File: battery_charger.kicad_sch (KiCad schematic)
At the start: 29 parts, among them J8 Conn_01x04, U15 BQ25895RTW, U17 NX3DV42GU, U18 MP3422GG-P, U20 MAX16150A

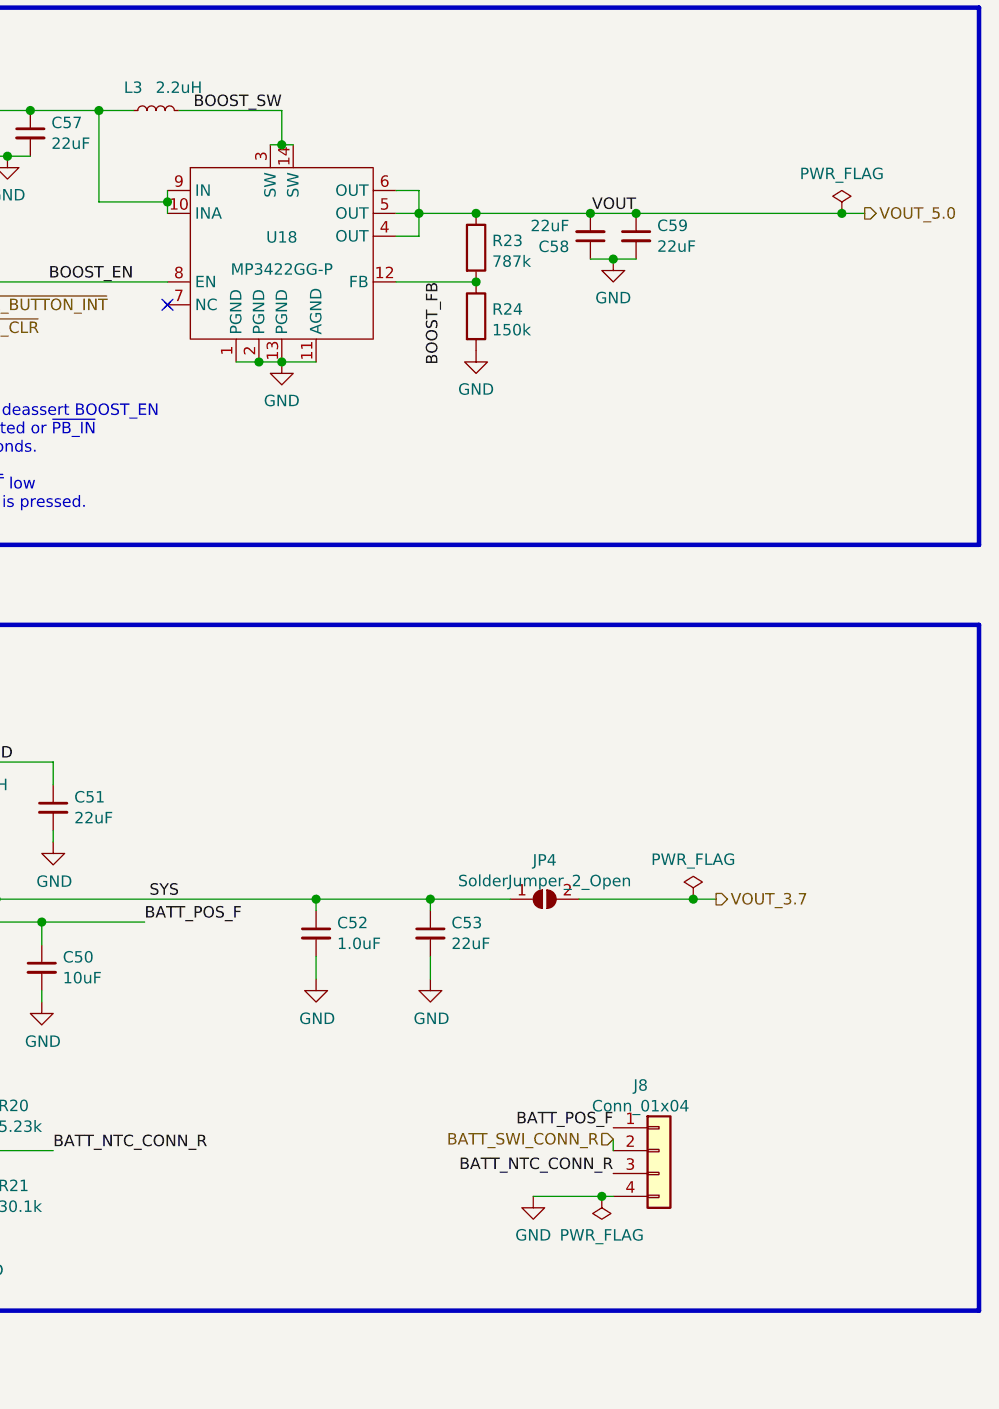
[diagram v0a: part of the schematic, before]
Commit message: Fix most ERC errors; cleanup silkscreen and comment layers.
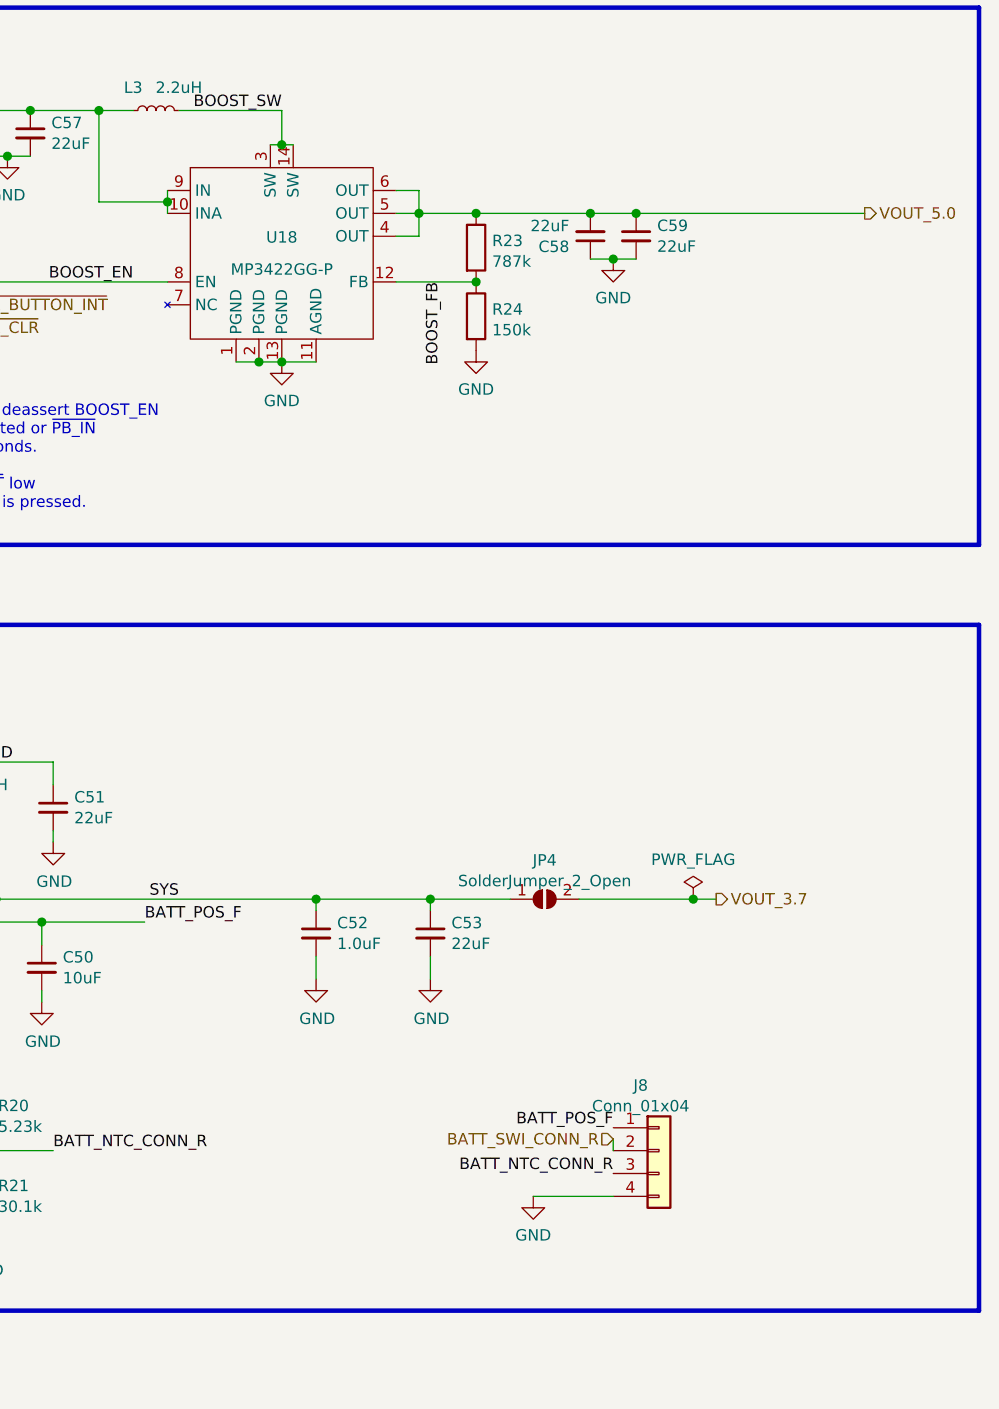
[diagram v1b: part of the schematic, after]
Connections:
- no-connect marks 1 -> 0
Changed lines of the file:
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@@
   (junction (at 238.76 48.26) (diameter 1.016) (color 0 0 0 0)
   )
-  (junction (at 237.49 152.4) (diameter 1.016) (color 0 0 0 0)
-  )
   (junction (at 165.1 119.38) (diameter 1.016) (color 0 0 0 0)
   )
   (junction (at 218.44 119.38) (diameter 1.016) (color 0 0 0 0)
   )
-  (junction (at 264.16 43.18) (diameter 1.016) (color 0 0 0 0)
-  )
   (junction (at 201.93 59.69) (diameter 1.016) (color 0 0 0 0)
   )
@@
   (junction (at 199.39 59.69) (diameter 1.016) (color 0 0 0 0)
   )
-  (no_connect (at 189.23 53.34))
   (polyline (pts (xy 279.4 80.01) (xy 113.03 80.01))
     (stroke (width 0.5) (type default) (color 0 0 0 0))
@@
     (stroke (width 0) (type solid) (color 0 0 0 0))
   )
-  (wire (pts (xy 229.87 152.4) (xy 237.49 152.4))
-    (stroke (width 0) (type solid) (color 0 0 0 0))
-  )
-  (wire (pts (xy 237.49 152.4) (xy 238.76 152.4))
+  (wire (pts (xy 229.87 152.4) (xy 238.76 152.4))
     (stroke (width 0) (type solid) (color 0 0 0 0))
   )
@@
     (stroke (width 0) (type solid) (color 0 0 0 0))
   )
-  (wire (pts (xy 241.3 43.18) (xy 264.16 43.18))
-    (stroke (width 0) (type solid) (color 0 0 0 0))
-  )
-  (wire (pts (xy 266.7 43.18) (xy 264.16 43.18))
+  (wire (pts (xy 241.3 43.18) (xy 266.7 43.18))
     (stroke (width 0) (type solid) (color 0 0 0 0))
   )
@@
   )
   (label "BOOST_FB" (at 219.71 50.8 270)
-    (effects (font (size 1.27 1.27)) (justify right bottom))
-  )
-  (label "VOUT" (at 241.3 43.18 180)
     (effects (font (size 1.27 1.27)) (justify right bottom))
   )
@@
     (pin "2")
   )
-  (symbol (lib_id "power:PWR_FLAG") (at 264.16 43.18 0) (unit 1)
-    (in_bom yes) (on_board yes)
-    (property "Reference" "#FLG0103" (id 0) (at 264.16 41.275 0)
-      (effects (font (size 1.27 1.27)) hide)
-    )
-    (property "Value" "PWR_FLAG" (id 1) (at 264.16 38.7858 0))
-    (property "Footprint" "" (id 2) (at 264.16 43.18 0)
-      (effects (font (size 1.27 1.27)) hide)
-    )
-    (property "Datasheet" "~" (id 3) (at 264.16 43.18 0)
-      (effects (font (size 1.27 1.27)) hide)
-    )
-    (pin "1")
-  )
   (symbol (lib_id "power:GND") (at 171.45 36.83 0) (unit 1)
     (in_bom yes) (on_board yes) (fields_autoplaced)
@@
       (effects (font (size 1.27 1.27)) hide)
     )
-    (pin "1")
-  )
-  (symbol (lib_id "power:PWR_FLAG") (at 237.49 152.4 180) (unit 1)
-    (in_bom yes) (on_board yes) (fields_autoplaced)
-    (property "Reference" "#FLG0101" (id 0) (at 237.49 154.305 0)
-      (effects (font (size 1.27 1.27)) hide)
-    )
-    (property "Value" "PWR_FLAG" (id 1) (at 237.49 156.7244 0))
-    (property "Footprint" "" (id 2) (at 237.49 152.4 0)
-      (effects (font (size 1.27 1.27)) hide)
-    )
-    (property "Datasheet" "~" (id 3) (at 237.49 152.4 0)
-      (effects (font (size 1.27 1.27)) hide)
-    )

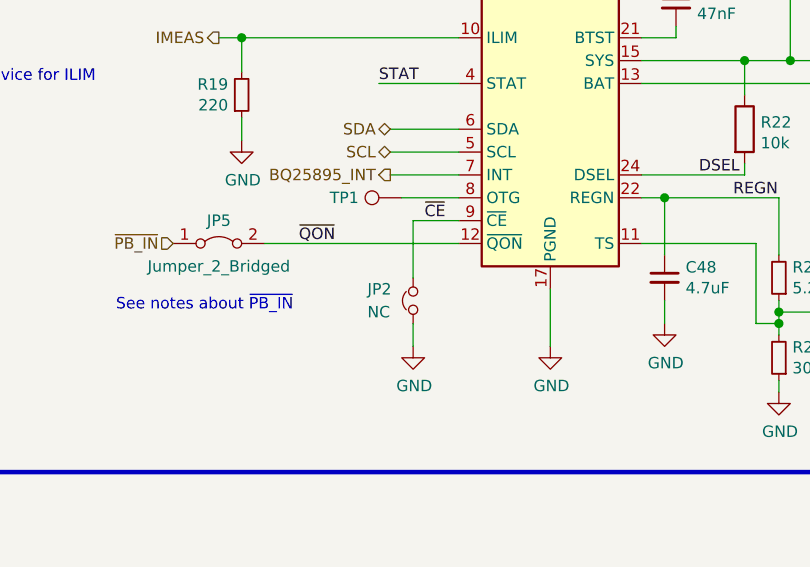
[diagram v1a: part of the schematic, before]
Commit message: Fix more ERC/DRC errors.
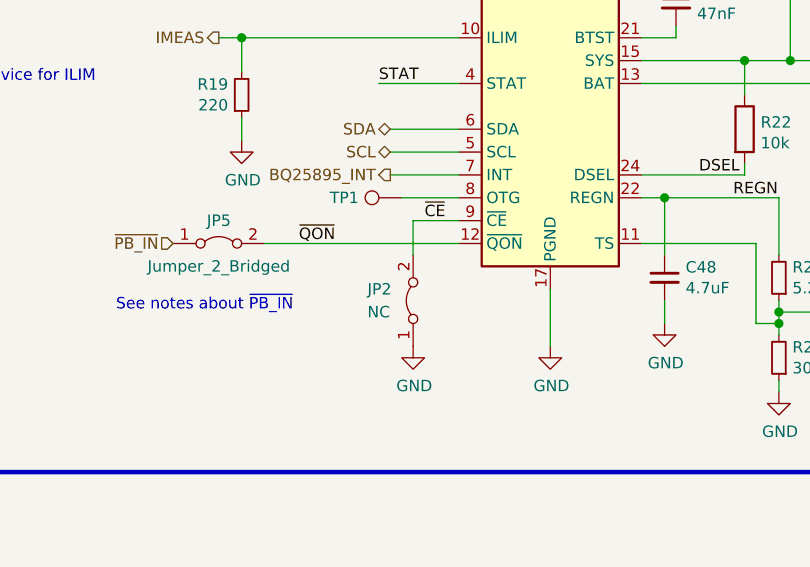
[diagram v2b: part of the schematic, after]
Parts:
- JP2: symbol Device:Jumper_NC_Small -> Jumper:Jumper_2_Bridged
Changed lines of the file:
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@@
-    (stroke (width 0) (type solid) (color 0 0 0 0))
-  )
-  (wire (pts (xy 128.27 148.59) (xy 128.27 151.13))
     (stroke (width 0) (type solid) (color 0 0 0 0))
   )
@@
     (stroke (width 0) (type solid) (color 0 0 0 0))
   )
-  (wire (pts (xy 128.27 137.16) (xy 128.27 143.51))
+  (wire (pts (xy 128.27 137.16) (xy 128.27 140.97))
     (stroke (width 0) (type solid) (color 0 0 0 0))
   )
@@
     (pin "1")
   )
-  (symbol (lib_id "Device:Jumper_NC_Small") (at 128.27 146.05 90) (unit 1)
+  (symbol (lib_id "Jumper:Jumper_2_Bridged") (at 128.27 146.05 90) (unit 1)
     (in_bom yes) (on_board yes)
     (property "Reference" "JP2" (id 0) (at 123.19 144.78 90)

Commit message: Board rev2 ready to order, hopefully
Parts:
- removed JP7: Jumper_2_Bridged, Resistor_SMD:R_0402_1005Metric, symbol Jumper:Jumper_2_Bridged
- added R26: 10k, Resistor_SMD:R_0402_1005Metric, symbol Device:R
- added R27: 20k, Resistor_SMD:R_0402_1005Metric, symbol Device:R
- added TP9: TestPoint, footprints:testpoint_small, symbol Connector:TestPoint
- TP1: footprint TestPoint:TestPoint_Pad_1.0x1.0mm -> footprints:testpoint_small
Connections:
- net ~{PB_IN}? is gone; now on net ~{PB_IN}: U20.1 (~{PB_IN})
- net GND: now also R27.2
- net STAT: now also TP9.1
- net VOUT_5.0: now also R26.1
- net ~{PWR_CLR}: now also R26.2, R27.1
- net OTG: now reaches TP1.1, U15.8 (OTG)
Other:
- note added: "5v Boost and power button"
- note added: "dtoverlay=gpio-shutdown,gpio_pin=22,active_low=1,gpio_pull=up,debounce=10 dtoverlay=gpio-poweroff,gpiopin=17,active_low=1"
- note removed: "5v Boost"
- moved on the sheet: C56, C57, C58, C59, L3, R23, R24, U18, U20
